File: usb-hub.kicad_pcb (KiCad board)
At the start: 4 copper layers, 23.4 x 28.4 mm, 61 parts, among them J1 USB_C_Receptacle_16pin, J2 USB_C_Receptacle_16pin, J3 USB_C_Receptacle_16pin, J4 Conn_01x01_Female, J5 Conn_01x01_Female, J6 Conn_01x01_Female, J7 Conn_01x01_Female, Q1 PMOS, -3.6A, 0.02R, Q2 Q_NMOS_GSD 1Amp, Q3 Q_NMOS_GSD 1Amp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

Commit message: fixed reset filter
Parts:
- C1, C4, C5, C6: value 1uF, ceramic, 6v, 10%, x5r -> 1uF, ceramic, 10v, 10%, x5r
- C2, C3: value 20pf, ceramic, 6v, 5% -> 20pF, ceramic, 100v, 5%
- C7, C8: value 10uF, ceramic, 6v, 10%, x5r -> 10uF, ceramic, 10v, 10%, x5r
- C9: value 100pF ceramic, 100v, 10% -> 1uF, ceramic, 10v, 10%, x5r
- R7: value 10k, 125mW, 5% -> 5.1k, 125mW, 5%
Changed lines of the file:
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@@
       (effects (font (size 0.7 0.7) (thickness 0.1)) (justify mirror))
     )
-    (fp_text value "20pf, ceramic, 6v, 5%" (at 0 -1.5 180) (layer B.Fab) hide
+    (fp_text value "20pF, ceramic, 100v, 5%" (at 0 -1.5 180) (layer B.Fab) hide
       (effects (font (size 1 1) (thickness 0.15)) (justify mirror))
     )
@@
       (effects (font (size 0.7 0.7) (thickness 0.1)) (justify mirror))
     )
-    (fp_text value "10uF, ceramic, 6v, 10%, x5r" (at 0 -1.5 180) (layer B.Fab) hide
+    (fp_text value "10uF, ceramic, 10v, 10%, x5r" (at 0 -1.5 180) (layer B.Fab) hide
       (effects (font (size 1 1) (thickness 0.15)) (justify mirror))
     )
@@
       (effects (font (size 0.7 0.7) (thickness 0.1)))
     )
-    (fp_text value "1uF, ceramic, 6v, 10%, x5r" (at 0 1.5) (layer F.Fab) hide
+    (fp_text value "1uF, ceramic, 10v, 10%, x5r" (at 0 1.5) (layer F.Fab) hide
       (effects (font (size 1 1) (thickness 0.15)))
     )
@@
       (effects (font (size 0.7 0.7) (thickness 0.1)) (justify mirror))
     )
-    (fp_text value "10uF, ceramic, 6v, 10%, x5r" (at 0 -1.5) (layer B.Fab) hide
+    (fp_text value "10uF, ceramic, 10v, 10%, x5r" (at 0 -1.5) (layer B.Fab) hide
       (effects (font (size 1 1) (thickness 0.15)) (justify mirror))
     )
@@
       (effects (font (size 0.7 0.7) (thickness 0.1)) (justify mirror))
     )
-    (fp_text value "20pf, ceramic, 6v, 5%" (at 0 -1.5 270) (layer B.Fab) hide
+    (fp_text value "20pF, ceramic, 100v, 5%" (at 0 -1.5 270) (layer B.Fab) hide
       (effects (font (size 1 1) (thickness 0.15)) (justify mirror))
     )
@@
       (effects (font (size 0.7 0.7) (thickness 0.1)))
     )
-    (fp_text value "1uF, ceramic, 6v, 10%, x5r" (at 0 1.5 180) (layer F.Fab) hide
+    (fp_text value "1uF, ceramic, 10v, 10%, x5r" (at 0 1.5 180) (layer F.Fab) hide
       (effects (font (size 0.127 1) (thickness 0.03175)))
     )
@@
       (effects (font (size 0.7 0.7) (thickness 0.1)) (justify mirror))
     )
-    (fp_text value "1uF, ceramic, 6v, 10%, x5r" (at 0 -1.5 270) (layer B.Fab) hide
+    (fp_text value "1uF, ceramic, 10v, 10%, x5r" (at 0 -1.5 270) (layer B.Fab) hide
       (effects (font (size 1 1) (thickness 0.15)) (justify mirror))
     )
@@
       (effects (font (size 0.7 0.7) (thickness 0.1)))
     )
-    (fp_text value "1uF, ceramic, 6v, 10%, x5r" (at 0 1.5 90) (layer F.Fab) hide
+    (fp_text value "1uF, ceramic, 10v, 10%, x5r" (at 0 1.5 90) (layer F.Fab) hide
       (effects (font (size 1 1) (thickness 0.15)))
     )
@@
       (effects (font (size 0.6 0.6) (thickness 0.1)) (justify mirror))
     )
-    (fp_text value "10k, 125mW, 5%" (at 0 -1.5 90) (layer B.Fab) hide
+    (fp_text value "5.1k, 125mW, 5%" (at 0 -1.5 90) (layer B.Fab) hide
       (effects (font (size 1 1) (thickness 0.15)) (justify mirror))
     )
@@
       (effects (font (size 0.7 0.7) (thickness 0.1)))
     )
-    (fp_text value "100pF ceramic, 100v, 10%" (at 0 1.5) (layer F.Fab)
-      (effects (font (size 1 1) (thickness 0.15)))
-    )
+    (fp_text value "1uF, ceramic, 10v, 10%, x5r" (at 0 1.5) (layer F.Fab)
+      (effects (font (size 1 1) (thickness 0.15)))
+    )

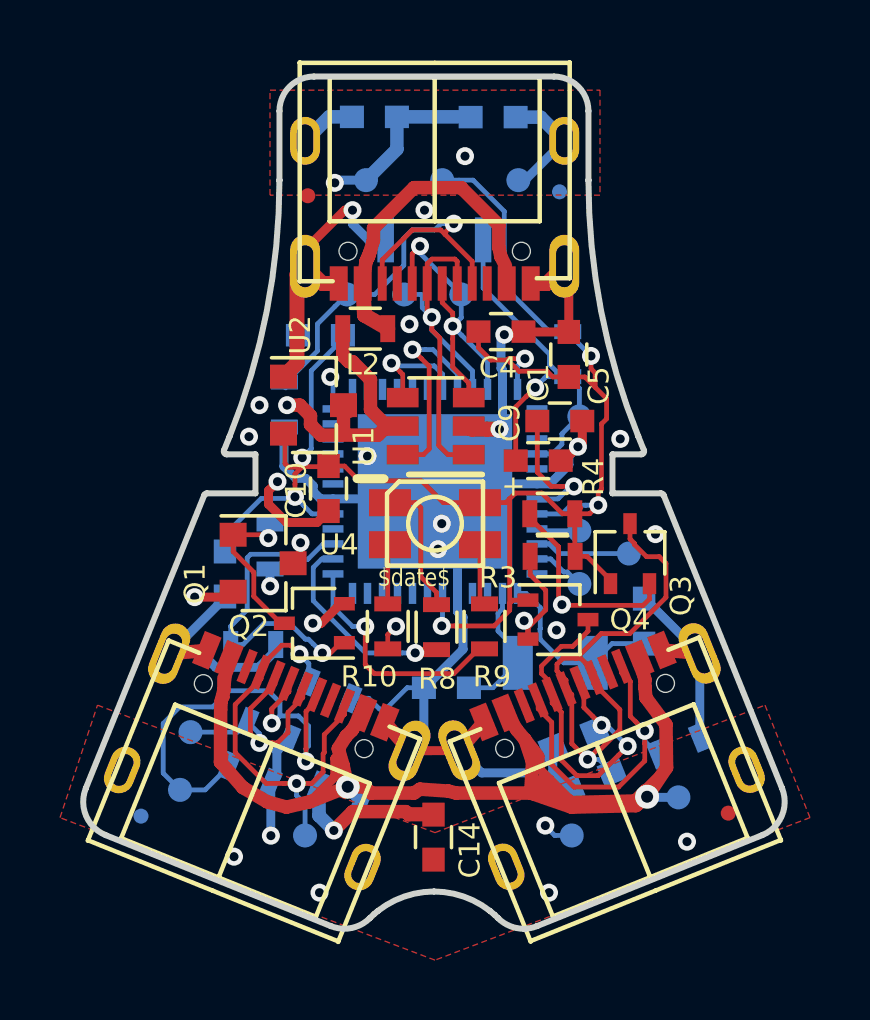
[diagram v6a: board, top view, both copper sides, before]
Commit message: ESD fixes recommmended by ASIM. Also better caps distribution
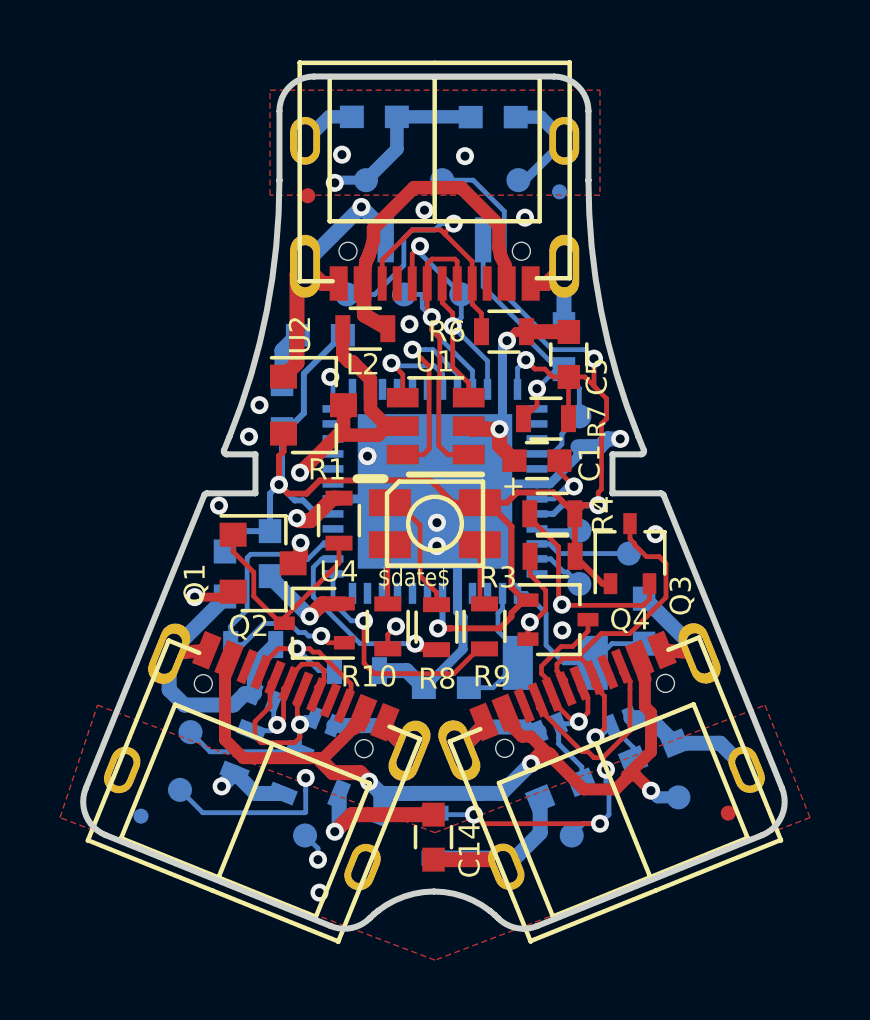
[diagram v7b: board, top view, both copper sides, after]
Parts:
- added D1: ESD-diode, raise_fp:sod882, B.Cu at (145.8, 113.5)
- added D2: ESD-diode, raise_fp:sod882, B.Cu at (138.3, 113.3)
- added D3: ESD-diode, raise_fp:sod882, B.Cu at (148.2, 113.3)
- added D4: ESD-diode, raise_fp:sod882, B.Cu at (136.3, 112.5)
- C10, C4, C9: moved to B.Cu
- R1, R6, R7: moved to F.Cu
- moved R11 8.66 mm to (142.0, 117.1), turned to 270 degrees
- moved C4 7.72 mm to (136.9, 102.8), turned to 90 degrees
- moved R6 7.71 mm to (144.3, 100.3), turned to 0 degrees
- moved C9 3.90 mm to (146.3, 100.8), turned to 90 degrees
- moved C10 2.92 mm to (136.5, 107.7)
- moved R1 2.46 mm to (138.8, 106.6), turned to 270 degrees
- moved C12 2.31 mm to (149.3, 114.3), turned to 202 degrees
- moved R7 2.27 mm to (145.7, 103.2), turned to 0 degrees
- moved C11 1.77 mm to (146.2, 115.6)
- moved R13 1.60 mm to (137.2, 115.0), turned to 248 degrees
- moved C1 1.52 mm to (145.4, 104.6), turned to 0 degrees
- moved R12 1.11 mm to (139.4, 111.6), turned to 0 degrees
- moved R14 0.79 mm to (135.6, 114.3), turned to 248 degrees
- moved L1 0.74 mm to (139.5, 116.0)
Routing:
- net +5V: track 61.6 -> 45.3 mm
- net /side-power: track 46.4 -> 30.3 mm, vias 2 -> 3
- net /scl: track 52.8 -> 38.2 mm
- net /sda: track 42.2 -> 29.5 mm, vias 3 -> 2
- net /side-power-pre-ferrite: track 21.6 -> 17.7 mm
- net /dfp-l-cc: track 13.9 -> 16.9 mm
- net Earth: track 111.0 -> 108.3 mm, vias 21 -> 19
- net /ufp-cc: track 14.9 -> 12.7 mm
- net +3V3: track 58.5 -> 60.6 mm, vias 6 -> 5
- net Net-(C1-Pad2): track 4.53 -> 2.55 mm
- net Net-(Q1-Pad1): track 5.81 -> 7.52 mm, vias 1 -> 0
- net /reset: track 13.4 -> 11.7 mm
- net /dfp-r-cc: track 16.9 -> 16.0 mm, vias 2 -> 3
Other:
- net class +5v: trace_width 0.3 -> 0.5
- net class 3.3v added: clearance 0.16, trace_width 0.2, via_dia 0.6, via_drill 0.3
- board text added: "keep outs"
